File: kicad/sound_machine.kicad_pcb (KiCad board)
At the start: 2 copper layers, 13 parts, among them J1 Conn_01x02, J2 Conn_01x15, J3 Conn_01x15, J4 TEST_1P, J5 Audio-Jack-3, J6 TEST_1P, J7 TEST_1P, J8 TEST_1P, U1 MPU-6050_breakout, U2 DFPlayerMini

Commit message: Basic layout
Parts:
- U2: footprint Socket_Strips:Socket_Strip_Straight_2x08_Pitch2.54mm -> DFPlayerMini
- moved LS1 58.1 mm to (124.5, 52.1), turned to 90 degrees
- moved J8 54.4 mm to (135.9, 52.1)
- moved J5 50.8 mm to (177.8, 63.5), turned to 270 degrees
- moved J7 49.5 mm to (135.9, 57.1)
- moved J6 47.0 mm to (135.9, 59.7)
- moved J4 44.6 mm to (135.9, 62.2)
- moved J1 42.4 mm to (151.1, 147.3), turned to 270 degrees
- moved U2 35.3 mm to (151.1, 69.8), turned to 180 degrees
- moved R1 29.8 mm to (162.6, 78.7)
- moved U1 12.4 mm to (157.5, 96.5), turned to 180 degrees
- moved J3 9.92 mm to (157.5, 109.2)
- moved J2 7.55 mm to (142.2, 109.2)
- moved R2 6.32 mm to (142.2, 104.1), turned to 270 degrees
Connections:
- U2 pad 10: Net-(U2-Pad10) -> GND
- U2 pad 11: Net-(U2-Pad11) -> Net-(J7-Pad1)
- U2 pad 12: Net-(J4-Pad1) -> Net-(J6-Pad1)
- U2 pad 13: Net-(J6-Pad1) -> Net-(J4-Pad1)
- U2 pad 14: Net-(J7-Pad1) -> Net-(U2-Pad14)
- U2 pad 15: GND -> Net-(U2-Pad15)
- U2 pad 16: Net-(J8-Pad1) -> Net-(U2-Pad16)
- U2 pad 9: Net-(U2-Pad9) -> Net-(J8-Pad1)
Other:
- board outline added: 100 x 100 mm
- net class Default: clearance 0.2 -> 0.1524; trace_width 0.25 -> 0.1524; via_dia 0.6 -> 0.6858; via_drill 0.4 -> 0.3302
- rule trace_clearance: 0.2 -> 0.1524
- rule trace_min: 0.2 -> 0.1524
- rule via_min_drill: 0.3 -> 0.3302
- rule via_min_size: 0.4 -> 0.6858

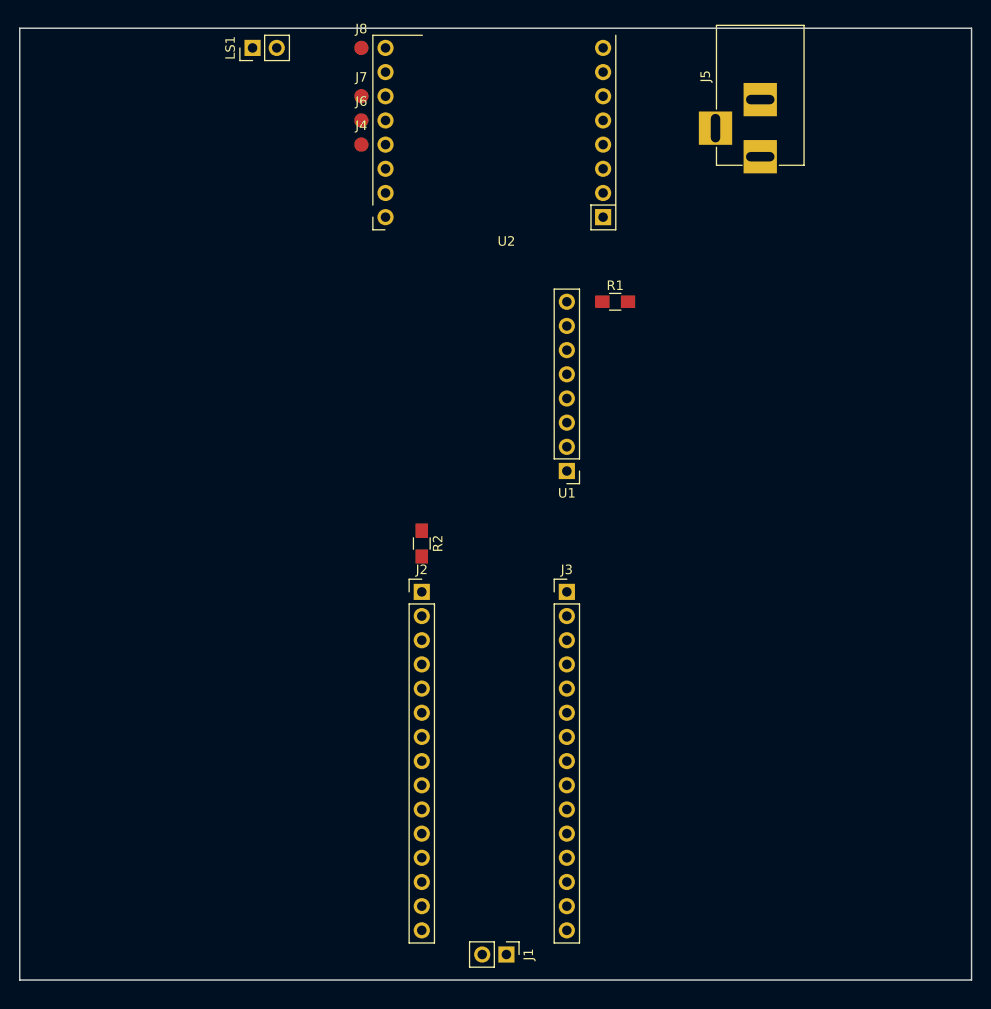
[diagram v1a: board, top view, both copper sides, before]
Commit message: Mounting holes
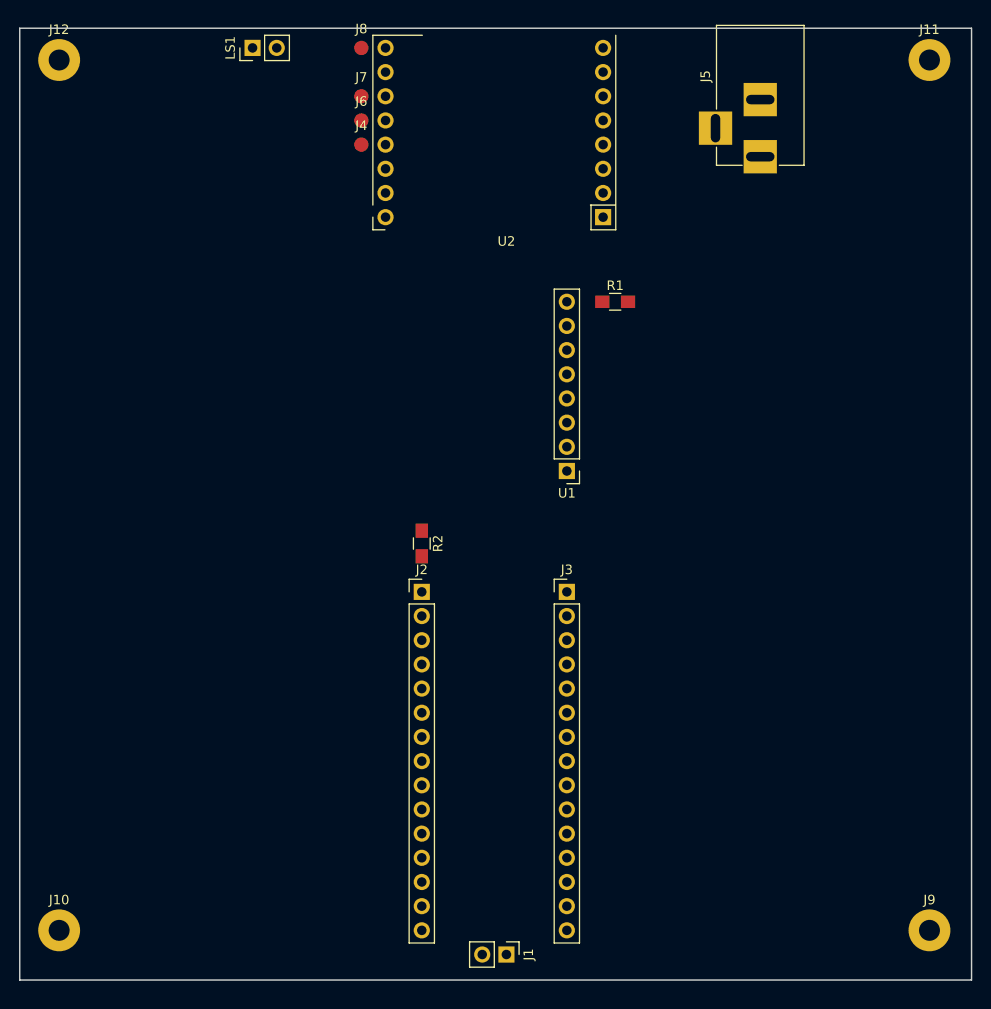
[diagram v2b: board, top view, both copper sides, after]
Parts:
- added J10: Conn_01x01, Mounting_Holes:MountingHole_2.2mm_M2_Pad, F.Cu at (104.1, 144.8)
- added J11: Conn_01x01, Mounting_Holes:MountingHole_2.2mm_M2_Pad, F.Cu at (195.6, 53.3)
- added J12: Conn_01x01, Mounting_Holes:MountingHole_2.2mm_M2_Pad, F.Cu at (104.1, 53.3)
- added J9: Conn_01x01, Mounting_Holes:MountingHole_2.2mm_M2_Pad, F.Cu at (195.6, 144.8)
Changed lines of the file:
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@@
 (kicad_pcb (version 4) (host pcbnew 4.0.7-e2-6376~58~ubuntu16.04.1)
   (general
-    (links 0)
-    (no_connects 25)
+    (links 29)
+    (no_connects 26)
     (area 99.924999 49.924999 200.075001 150.075001)
     (thickness 1.6)
@@
     (tracks 0)
     (zones 0)
-    (modules 13)
+    (modules 17)
     (nets 45)
   )
@@
     )
   )
+  (module Mounting_Holes:MountingHole_2.2mm_M2_Pad (layer F.Cu)
+    (at 195.58 144.78)
+    (descr "Mounting Hole 2.2mm, M2")
+    (tags "mounting hole 2.2mm m2")
+    (fp_text reference J9 (at 0 -3.2) (layer F.SilkS)
+      (effects (font (size 1 1) (thickness 0.15)))
+    )
+    (fp_text value Conn_01x01 (at 0 3.2) (layer F.Fab)
+      (effects (font (size 1 1) (thickness 0.15)))
+    )
+    (fp_circle (center 0 0) (end 2.2 0) (layer Cmts.User) (width 0.15))
+    (fp_circle (center 0 0) (end 2.45 0) (layer F.CrtYd) (width 0.05))
+    (pad 1 thru_hole circle (at 0 0) (size 4.4 4.4) (drill 2.2) (layers *.Cu *.Mask)
+      (net 2 GND))
+  )
+  (module Mounting_Holes:MountingHole_2.2mm_M2_Pad (layer F.Cu)
+    (at 104.14 144.78)
+    (descr "Mounting Hole 2.2mm, M2")
+    (tags "mounting hole 2.2mm m2")
+    (fp_text reference J10 (at 0 -3.2) (layer F.SilkS)
+      (effects (font (size 1 1) (thickness 0.15)))
+    )
+    (fp_text value Conn_01x01 (at 0 3.2) (layer F.Fab)
+      (effects (font (size 1 1) (thickness 0.15)))
+    )
+    (fp_circle (center 0 0) (end 2.2 0) (layer Cmts.User) (width 0.15))
+    (fp_circle (center 0 0) (end 2.45 0) (layer F.CrtYd) (width 0.05))
+    (pad 1 thru_hole circle (at 0 0) (size 4.4 4.4) (drill 2.2) (layers *.Cu *.Mask)
+      (net 2 GND))
+  )
+  (module Mounting_Holes:MountingHole_2.2mm_M2_Pad (layer F.Cu)
+    (at 195.58 53.34)
+    (descr "Mounting Hole 2.2mm, M2")
+    (tags "mounting hole 2.2mm m2")
+    (fp_text reference J11 (at 0 -3.2) (layer F.SilkS)
+      (effects (font (size 1 1) (thickness 0.15)))
+    )
+    (fp_text value Conn_01x01 (at 0 3.2) (layer F.Fab)
+      (effects (font (size 1 1) (thickness 0.15)))
+    )
+    (fp_circle (center 0 0) (end 2.2 0) (layer Cmts.User) (width 0.15))
+    (fp_circle (center 0 0) (end 2.45 0) (layer F.CrtYd) (width 0.05))
+    (pad 1 thru_hole circle (at 0 0) (size 4.4 4.4) (drill 2.2) (layers *.Cu *.Mask)
+      (net 2 GND))
+  )
+  (module Mounting_Holes:MountingHole_2.2mm_M2_Pad (layer F.Cu)
+    (at 104.14 53.34)
+    (descr "Mounting Hole 2.2mm, M2")
+    (tags "mounting hole 2.2mm m2")
+    (fp_text reference J12 (at 0 -3.2) (layer F.SilkS)
+      (effects (font (size 1 1) (thickness 0.15)))
+    )
+    (fp_text value Conn_01x01 (at 0 3.2) (layer F.Fab)
+      (effects (font (size 1 1) (thickness 0.15)))
+    )
+    (fp_circle (center 0 0) (end 2.2 0) (layer Cmts.User) (width 0.15))
+    (fp_circle (center 0 0) (end 2.45 0) (layer F.CrtYd) (width 0.05))
+    (pad 1 thru_hole circle (at 0 0) (size 4.4 4.4) (drill 2.2) (layers *.Cu *.Mask)
+      (net 2 GND))
+  )
   (dimension 50 (width 0.3) (layer Cmts.User)

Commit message: Nano expansion
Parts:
- added J13: Conn_01x15, Pin_Headers:Pin_Header_Straight_1x15_Pitch2.54mm, F.Cu at (139.7, 109.2)
- added J14: Conn_01x15, Pin_Headers:Pin_Header_Straight_1x15_Pitch2.54mm, F.Cu at (137.2, 109.2)
- added J15: Conn_01x15, Pin_Headers:Pin_Header_Straight_1x15_Pitch2.54mm, F.Cu at (134.6, 109.2)
- added J16: Conn_01x15, Pin_Headers:Pin_Header_Straight_1x15_Pitch2.54mm, F.Cu at (160.0, 109.2)
- added J17: Conn_01x15, Pin_Headers:Pin_Header_Straight_1x15_Pitch2.54mm, F.Cu at (162.6, 109.2)
- added J18: Conn_01x15, Pin_Headers:Pin_Header_Straight_1x15_Pitch2.54mm, F.Cu at (165.1, 109.2)
- moved R2 39.9 mm to (157.5, 67.3), turned to 180 degrees

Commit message: Connected
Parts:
- removed J7, J8: TEST_1P, Measurement_Points:Measurement_Point_Round-SMD-Pad_Small
- added J19: Conn_02x25_Counter_Clockwise, Pin_Headers:Pin_Header_Straight_2x25_Pitch2.54mm, F.Cu at (124.5, 71.1)
- added J20: Conn_02x25_Counter_Clockwise, Pin_Headers:Pin_Header_Straight_2x25_Pitch2.54mm, F.Cu at (119.4, 71.1)
- added J21: Conn_02x25_Counter_Clockwise, Pin_Headers:Pin_Header_Straight_2x25_Pitch2.54mm, F.Cu at (114.3, 71.1)
- added J22: Conn_02x25_Counter_Clockwise, Pin_Headers:Pin_Header_Straight_2x25_Pitch2.54mm, F.Cu at (172.7, 71.1)
- added J23: Conn_02x25_Counter_Clockwise, Pin_Headers:Pin_Header_Straight_2x25_Pitch2.54mm, F.Cu at (177.8, 71.1)
- added J24: Conn_02x25_Counter_Clockwise, Pin_Headers:Pin_Header_Straight_2x25_Pitch2.54mm, F.Cu at (182.9, 71.1)
- added J25: Conn_02x25_Counter_Clockwise, Pin_Headers:Pin_Header_Straight_2x25_Pitch2.54mm, F.Cu at (109.2, 71.1)
- added J26: Conn_02x25_Counter_Clockwise, Pin_Headers:Pin_Header_Straight_2x25_Pitch2.54mm, F.Cu at (188.0, 71.1)
- J4, J6: value TEST_1P -> Conn_01x08; footprint Measurement_Points:Measurement_Point_Round-SMD-Pad_Small -> Pin_Headers:Pin_Header_Straight_1x08_Pitch2.54mm
- U2: footprint DFPlayerMini -> sound_machine:DFPlayerMini
- moved J4 29.0 mm to (163.8, 69.8), turned to 180 degrees
- moved J6 10.2 mm to (135.9, 69.8), turned to 180 degrees
- moved R2 5.08 mm to (157.5, 72.4)
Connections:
- J16 pad 3: RST -> RESET
- J17 pad 3: RST -> RESET
- J18 pad 3: RST -> RESET
- J3 pad 3: RST -> RESET
- J4 pad 1: Net-(J4-Pad1) -> +5V
- J5 pad 1: Net-(J5-Pad1) -> Net-(J4-Pad5)
- J5 pad 2: Net-(J5-Pad2) -> Net-(J4-Pad4)
- LS1 pad 1: Net-(LS1-Pad1) -> Net-(J4-Pad6)
- LS1 pad 2: Net-(LS1-Pad2) -> Net-(J4-Pad8)
- R2 pad 1: Net-(R2-Pad1) -> Net-(J4-Pad2)
- U2 pad 11: Net-(J7-Pad1) -> Net-(J6-Pad6)
- U2 pad 12: Net-(J6-Pad1) -> Net-(J6-Pad5)
- U2 pad 13: Net-(J4-Pad1) -> Net-(J6-Pad4)
- U2 pad 14: Net-(U2-Pad14) -> Net-(J6-Pad3)
- U2 pad 15: Net-(U2-Pad15) -> Net-(J6-Pad2)
- U2 pad 16: Net-(U2-Pad16) -> Net-(J6-Pad1)
- U2 pad 2: Net-(R2-Pad1) -> Net-(J4-Pad2)
- U2 pad 4: Net-(J5-Pad2) -> Net-(J4-Pad4)
- U2 pad 5: Net-(J5-Pad1) -> Net-(J4-Pad5)
- U2 pad 6: Net-(LS1-Pad1) -> Net-(J4-Pad6)
- U2 pad 8: Net-(LS1-Pad2) -> Net-(J4-Pad8)
- U2 pad 9: Net-(J8-Pad1) -> Net-(J6-Pad8)
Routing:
- net GND: track 0.00 -> 535.3 mm
- net RX0: track 0.00 -> 70.0 mm
- net +5V: track 0.00 -> 65.0 mm
- net D2: track 0.00 -> 63.7 mm
- net Net-(J4-Pad6): track 0.00 -> 62.4 mm
- net Net-(J4-Pad8): track 0.00 -> 61.8 mm
- net TX1: track 0.00 -> 54.0 mm
- net SDA: track 0.00 -> 49.0 mm
- net VIN: track 0.00 -> 49.0 mm
- net SCL: track 0.00 -> 43.1 mm
- net Net-(J4-Pad4): track 0.00 -> 30.9 mm
- net Net-(J4-Pad5): track 0.00 -> 18.1 mm
- net Net-(J4-Pad2): track 0.00 -> 9.34 mm
- net RST: track 0.00 -> 7.62 mm
- net RESET: track 0.00 -> 7.62 mm
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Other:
- net class 3v added: clearance 0.508, trace_width 0.508, via_dia 0.6858, via_drill 0.3302
- net class 5v added: clearance 0.508, trace_width 0.508, via_dia 0.6858, via_drill 0.3302
- net class Default: clearance 0.1524 -> 0.2032; trace_width 0.1524 -> 0.2032
- rule trace_clearance: 0.1524 -> 0.2032

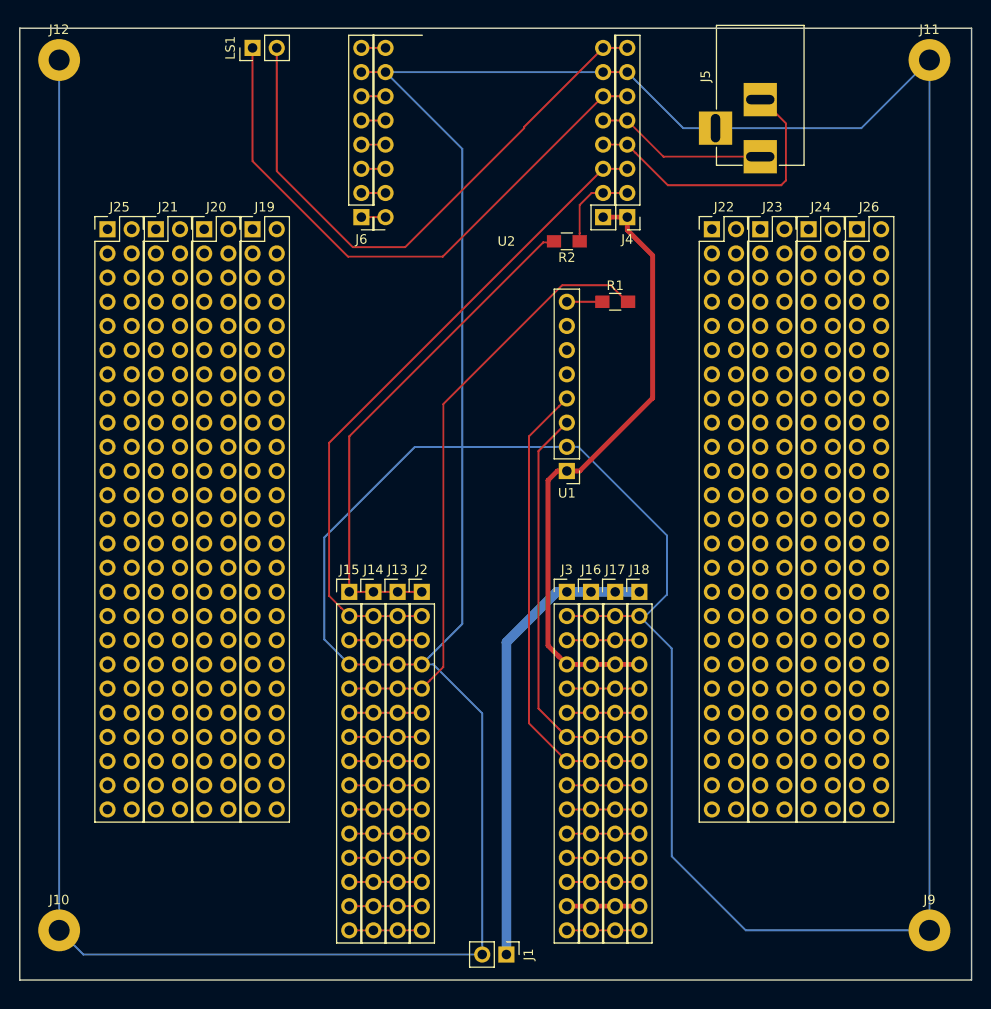
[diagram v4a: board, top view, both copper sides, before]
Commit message: Smaller board
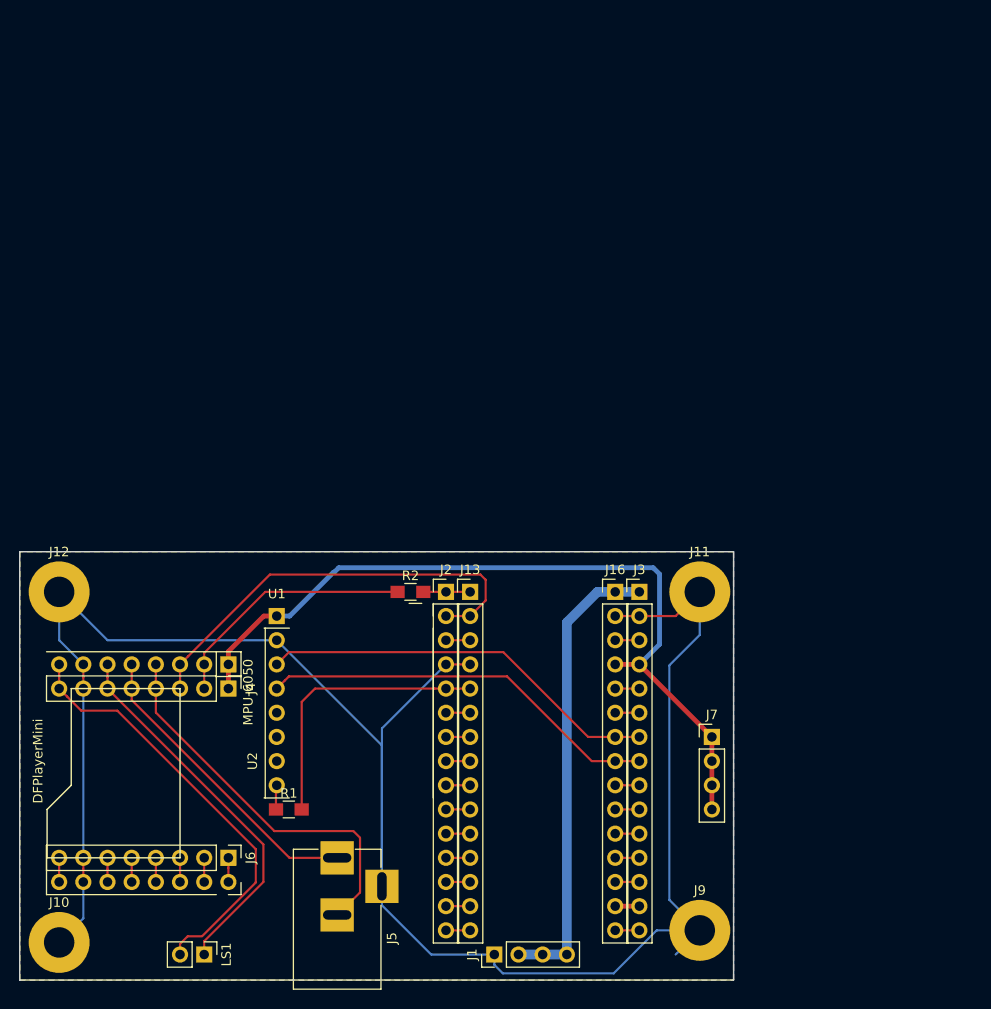
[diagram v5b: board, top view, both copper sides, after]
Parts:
- removed J14, J15, J17, J18: Conn_01x15, Pin_Headers:Pin_Header_Straight_1x15_Pitch2.54mm
- removed J19, J20, J21, J22, J23, J24, J25, J26: Conn_02x25_Counter_Clockwise, Pin_Headers:Pin_Header_Straight_2x25_Pitch2.54mm
- added J7: Conn_01x04, Pin_Headers:Pin_Header_Straight_1x04_Pitch2.54mm, F.Cu at (172.7, 124.5)
- J1: value Conn_01x02 -> Conn_01x04; footprint Pin_Headers:Pin_Header_Straight_1x02_Pitch2.54mm -> Pin_Headers:Pin_Header_Straight_1x04_Pitch2.54mm
- J10, J11, J12, J9: footprint Mounting_Holes:MountingHole_2.2mm_M2_Pad -> Mounting_Holes:MountingHole_3.2mm_M3_Pad
- U1: footprint Pin_Headers:Pin_Header_Straight_1x08_Pitch2.54mm -> sound_machine:MPU-6050
- moved LS1 95.4 mm to (119.4, 147.3), turned to 270 degrees
- moved J5 86.0 mm to (133.3, 137.2), turned to 90 degrees
- moved J6 68.7 mm to (121.9, 137.2), turned to 270 degrees
- moved J4 64.9 mm to (121.9, 119.4), turned to 270 degrees
- moved U2 64.2 mm to (121.9, 127.0), turned to 270 degrees
- moved R1 63.4 mm to (128.3, 132.1)
- moved J11 60.9 mm to (171.4, 109.2)
- moved J12 55.9 mm to (104.1, 109.2)
- moved R2 40.3 mm to (141.1, 109.2), turned to 0 degrees
- moved U1 34.1 mm to (127.0, 111.8), turned to 0 degrees
- moved J9 24.1 mm to (171.4, 144.8)
- moved J13 7.62 mm to (147.3, 109.2)
- moved J3 7.62 mm to (165.1, 109.2)
- moved J16 2.54 mm to (162.6, 109.2)
- moved J2 2.54 mm to (144.8, 109.2)
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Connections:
- J1 pad 1: VIN -> GND
- J1 pad 2: GND -> VIN
- U1 pad 5: Net-(U1-Pad5) -> (no net)
- U1 pad 6: Net-(U1-Pad6) -> (no net)
- U1 pad 7: Net-(U1-Pad7) -> (no net)
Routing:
- net GND: track 535.3 -> 215.6 mm
- net TX1: track 54.0 -> 4.92 mm
- net D2: track 63.7 -> 29.6 mm
- net RX0: track 70.0 -> 45.8 mm
- net Net-(J4-Pad6): track 62.4 -> 39.8 mm
- net +5V: track 65.0 -> 84.4 mm
- net Net-(J4-Pad2): track 9.34 -> 26.7 mm
- net Net-(J4-Pad8): track 61.8 -> 45.4 mm
- net Net-(J4-Pad5): track 18.1 -> 32.6 mm
- net Net-(J4-Pad4): track 30.9 -> 41.1 mm
- net SDA: track 49.0 -> 42.3 mm
- net RST: track 7.62 -> 2.54 mm
- net RESET: track 7.62 -> 2.54 mm
- net D9: track 7.62 -> 2.54 mm
- net D8: track 7.62 -> 2.54 mm
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- added copper zone on B.Cu, net GND
- added copper zone on F.Cu, net GND
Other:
- board size 100 x 100 mm -> 75 x 45 mm
- net class Default: clearance 0.2032 -> 0.2286; trace_width 0.2032 -> 0.2286
- net class vin added: clearance 0.508, trace_width 1.016, via_dia 0.6858, via_drill 0.3302
- rule trace_clearance: 0.2032 -> 0.2286
